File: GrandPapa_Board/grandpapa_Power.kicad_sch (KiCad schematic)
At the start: 47 parts, among them J10 Conn_01x03_Female, J7 Conn_01x02_Female, J8 Conn_01x02_Female, J9 Conn_01x02_Female, U1 LD2985BM33R, U2 INA180A4QDBVRQ1, U3 INA180A4QDBVRQ1, U4 LT1576IS8-5#TRPBF, U5 FPF2124, U6 FPF2124, U7 FPF2124, U9 INA180A4QDBVRQ1

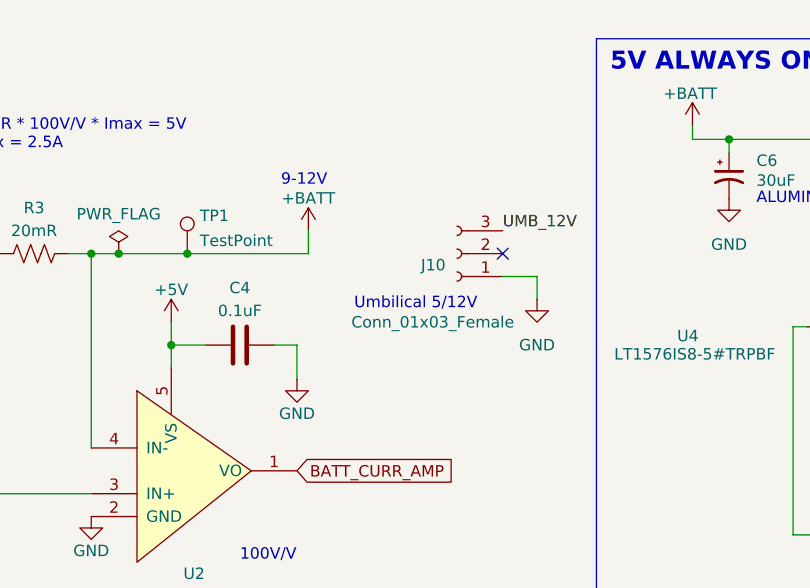
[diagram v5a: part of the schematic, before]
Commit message: Add FETs to power lines
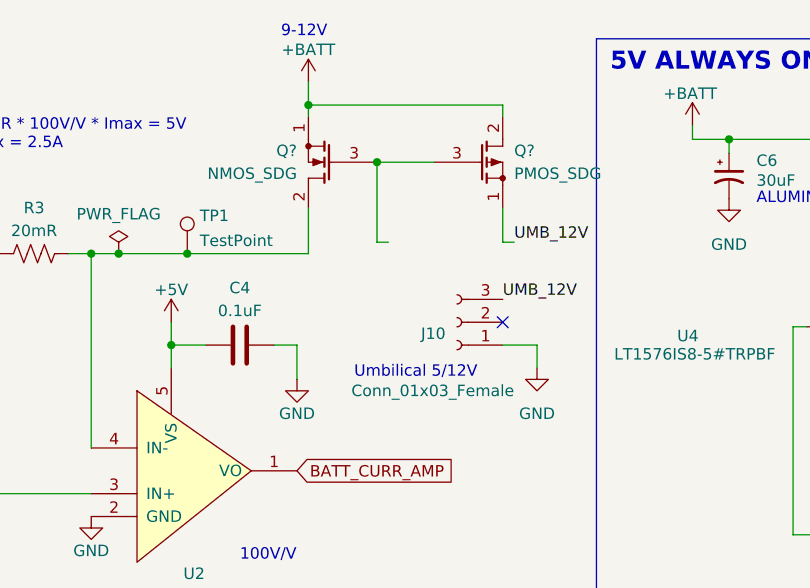
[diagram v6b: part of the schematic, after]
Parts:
- added Q?: PMOS_SDG, symbol CLEAN_MOS:PMOS_SDG
- added Q?: NMOS_SDG, symbol CLEAN_MOS:NMOS_SDG
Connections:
- net +BATT: now also Q?.1 (S), Q?.2 (D); no longer R3.1, TP1.1, U2.4 (IN-)
- net UMB_12V: now also Q?.1 (S)
- new net: Q?.2 (D), R3.1, TP1.1, U2.4 (IN-)
- new net: Q?.3 (G), Q?.3 (G)
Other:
- moved on the sheet: J10
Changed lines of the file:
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@@
   (junction (at 214.122 39.878) (diameter 0) (color 0 0 0 0)
   )
+  (junction (at 120.65 21.59) (diameter 0) (color 0 0 0 0)
+  )
   (junction (at 223.012 52.578) (diameter 0) (color 0 0 0 0)
   )
@@
   (junction (at 256.032 39.878) (diameter 0) (color 0 0 0 0)
   )
+  (junction (at 128.27 27.94) (diameter 0) (color 0 0 0 0)
+  )
   (junction (at 232.41 52.578) (diameter 0) (color 0 0 0 0)
   )
   (junction (at 83.82 38.1) (diameter 0) (color 0 0 0 0)
   )
-  (no_connect (at 142.24 38.1))
+  (no_connect (at 142.24 45.72))
   (wire (pts (xy 181.61 130.81) (xy 172.72 130.81))
     (stroke (width 0) (type default) (color 0 0 0 0))
@@
     (stroke (width 0) (type default) (color 0 0 0 0))
   )
+  (wire (pts (xy 142.24 33.02) (xy 142.24 36.83))
+    (stroke (width 0) (type default) (color 0 0 0 0))
+  )
+  (wire (pts (xy 120.65 19.05) (xy 120.65 21.59))
+    (stroke (width 0) (type default) (color 0 0 0 0))
+  )
   (wire (pts (xy 111.252 173.99) (xy 98.552 173.99))
     (stroke (width 0) (type default) (color 0 0 0 0))
@@
     (stroke (width 0) (type default) (color 0 0 0 0))
   )
-  (wire (pts (xy 142.24 40.64) (xy 146.05 40.64))
+  (wire (pts (xy 142.24 48.26) (xy 146.05 48.26))
     (stroke (width 0) (type default) (color 0 0 0 0))
   )
@@
     (stroke (width 0) (type default) (color 0 0 0 0))
   )
-  (wire (pts (xy 146.05 40.64) (xy 146.05 43.18))
+  (wire (pts (xy 146.05 48.26) (xy 146.05 50.8))
     (stroke (width 0) (type default) (color 0 0 0 0))
   )
@@
     (stroke (width 0) (type default) (color 0 0 0 0))
   )
+  (wire (pts (xy 128.27 27.94) (xy 134.62 27.94))
+    (stroke (width 0) (type default) (color 0 0 0 0))
+  )
   (wire (pts (xy 30.48 66.04) (xy 30.48 76.2))
     (stroke (width 0) (type default) (color 0 0 0 0))
@@
     (stroke (width 0) (type default) (color 0 0 0 0))
   )
+  (wire (pts (xy 120.65 21.59) (xy 142.24 21.59))
+    (stroke (width 0) (type default) (color 0 0 0 0))
+  )
   (wire (pts (xy 30.48 38.1) (xy 46.99 38.1))
     (stroke (width 0) (type default) (color 0 0 0 0))
@@
     (stroke (width 0) (type default) (color 0 0 0 0))
   )
+  (wire (pts (xy 120.65 21.59) (xy 120.65 22.86))
+    (stroke (width 0) (type default) (color 0 0 0 0))
+  )
   (wire (pts (xy 116.078 87.376) (xy 125.222 87.376))
     (stroke (width 0) (type default) (color 0 0 0 0))
@@
     (stroke (width 0) (type default) (color 0 0 0 0))
   )
+  (wire (pts (xy 142.24 22.86) (xy 142.24 21.59))
+    (stroke (width 0) (type default) (color 0 0 0 0))
+  )
+  (wire (pts (xy 142.24 36.83) (xy 143.51 36.83))
+    (stroke (width 0) (type default) (color 0 0 0 0))
+  )
   (wire (pts (xy 101.092 114.046) (xy 88.392 114.046))
     (stroke (width 0) (type default) (color 0 0 0 0))
@@
     (stroke (width 0) (type default) (color 0 0 0 0))
   )
+  (wire (pts (xy 128.27 36.83) (xy 129.54 36.83))
+    (stroke (width 0) (type default) (color 0 0 0 0))
+  )
   (wire (pts (xy 243.84 88.138) (xy 243.84 90.17))
     (stroke (width 0) (type default) (color 0 0 0 0))
@@
     (stroke (width 0) (type default) (color 0 0 0 0))
   )
-  (wire (pts (xy 120.65 35.56) (xy 120.65 38.1))
+  (wire (pts (xy 120.65 33.02) (xy 120.65 38.1))
     (stroke (width 0) (type default) (color 0 0 0 0))
   )
@@
   )
   (wire (pts (xy 107.188 38.1) (xy 120.65 38.1))
+    (stroke (width 0) (type default) (color 0 0 0 0))
+  )
+  (wire (pts (xy 128.27 27.94) (xy 128.27 36.83))
     (stroke (width 0) (type default) (color 0 0 0 0))
   )
@@
     (effects (font (size 1.27 1.27)) (justify left bottom))
   )
-  (text "Umbilical 5/12V" (at 125.73 44.45 0)
+  (text "Umbilical 5/12V" (at 125.73 52.07 0)
     (effects (font (size 1.27 1.27)) (justify left bottom))
   )
@@
     (effects (font (size 1.27 1.27)) (justify left bottom))
   )
-  (text "9-12V\n" (at 117.602 30.734 0)
+  (text "9-12V\n" (at 117.602 14.224 0)
     (effects (font (size 1.27 1.27)) (justify left bottom))
   )
@@
     (effects (font (size 1.27 1.27)) (justify left bottom))
   )
-  (label "UMB_12V" (at 142.24 35.56 0)
+  (label "UMB_12V" (at 142.24 43.18 0)
     (effects (font (size 1.27 1.27)) (justify left bottom))
   )
   (label "RAW_BATT" (at 74.168 35.306 180)
     (effects (font (size 1.27 1.27)) (justify right bottom))
+  )
+  (label "UMB_12V" (at 143.51 36.83 0)
+    (effects (font (size 1.27 1.27)) (justify left bottom))
   )
   (global_label "5V_LOGGER" (shape input) (at 243.84 88.138 0) (fields_autoplaced)
@@
     (pin "5")
   )
-  (symbol (lib_id "power:GND") (at 146.05 43.18 0) (unit 1)
-    (in_bom yes) (on_board yes) (fields_autoplaced)
-    (property "Reference" "#PWR08" (id 0) (at 146.05 49.53 0)
-      (effects (font (size 1.27 1.27)) hide)
-    )
-    (property "Value" "GND" (id 1) (at 146.05 48.26 0))
-    (property "Footprint" "" (id 2) (at 146.05 43.18 0)
-      (effects (font (size 1.27 1.27)) hide)
-    )
-    (property "Datasheet" "" (id 3) (at 146.05 43.18 0)
+  (symbol (lib_id "power:GND") (at 146.05 50.8 0) (unit 1)
+    (in_bom yes) (on_board yes) (fields_autoplaced)
+    (property "Reference" "#PWR08" (id 0) (at 146.05 57.15 0)
+      (effects (font (size 1.27 1.27)) hide)
+    )
+    (property "Value" "GND" (id 1) (at 146.05 55.88 0))
+    (property "Footprint" "" (id 2) (at 146.05 50.8 0)
+      (effects (font (size 1.27 1.27)) hide)
+    )
+    (property "Datasheet" "" (id 3) (at 146.05 50.8 0)
       (effects (font (size 1.27 1.27)) hide)
     )
@@
     (pin "5")
   )
+  (symbol (lib_id "CLEAN_MOS:PMOS_SDG") (at 139.7 27.94 0) (unit 1)
+    (in_bom yes) (on_board yes) (fields_autoplaced)
+    (property "Reference" "Q?" (id 0) (at 143.51 26.6699 0)
+      (effects (font (size 1.27 1.27)) (justify left))
+    )
+    (property "Value" "PMOS_SDG" (id 1) (at 143.51 29.2099 0)
+      (effects (font (size 1.27 1.27)) (justify left))
+    )
+    (property "Footprint" "" (id 2) (at 144.78 25.4 0)
+      (effects (font (size 1.27 1.27)) hide)
+    )
+    (property "Datasheet" "~" (id 3) (at 139.7 27.94 0)
+      (effects (font (size 1.27 1.27)) hide)
+    )
+    (pin "1")
+    (pin "2")
+    (pin "3")
+  )
   (symbol (lib_id "power:GND") (at 214.63 157.48 0) (unit 1)
     (in_bom yes) (on_board yes) (fields_autoplaced)
@@
     (pin "1")
   )
-  (symbol (lib_id "power:+BATT") (at 120.65 35.56 0) (unit 1)
-    (in_bom yes) (on_board yes) (fields_autoplaced)
-    (property "Reference" "#PWR015" (id 0) (at 120.65 39.37 0)
-      (effects (font (size 1.27 1.27)) hide)
-    )
-    (property "Value" "+BATT" (id 1) (at 120.65 31.9555 0))
-    (property "Footprint" "" (id 2) (at 120.65 35.56 0)
-      (effects (font (size 1.27 1.27)) hide)
-    )
-    (property "Datasheet" "" (id 3) (at 120.65 35.56 0)
+  (symbol (lib_id "power:+BATT") (at 120.65 19.05 0) (unit 1)
+    (in_bom yes) (on_board yes) (fields_autoplaced)
+    (property "Reference" "#PWR015" (id 0) (at 120.65 22.86 0)
+      (effects (font (size 1.27 1.27)) hide)
+    )
+    (property "Value" "+BATT" (id 1) (at 120.65 15.4455 0))
+    (property "Footprint" "" (id 2) (at 120.65 19.05 0)
+      (effects (font (size 1.27 1.27)) hide)
+    )
+    (property "Datasheet" "" (id 3) (at 120.65 19.05 0)
       (effects (font (size 1.27 1.27)) hide)
     )
@@
     (pin "1")
   )
-  (symbol (lib_id "Connector:Conn_01x03_Female") (at 137.16 38.1 180) (unit 1)
-    (in_bom yes) (on_board yes)
-    (property "Reference" "J10" (id 0) (at 135.89 39.3701 0)
-      (effects (font (size 1.27 1.27)) (justify left))
-    )
-    (property "Value" "Conn_01x03_Female" (id 1) (at 143.51 45.72 0)
-      (effects (font (size 1.27 1.27)) (justify left))
-    )
-    (property "Footprint" "" (id 2) (at 137.16 38.1 0)
-      (effects (font (size 1.27 1.27)) hide)
-    )
-    (property "Datasheet" "~" (id 3) (at 137.16 38.1 0)
+  (symbol (lib_id "Connector:Conn_01x03_Female") (at 137.16 45.72 180) (unit 1)
+    (in_bom yes) (on_board yes)
+    (property "Reference" "J10" (id 0) (at 135.89 46.9901 0)
+      (effects (font (size 1.27 1.27)) (justify left))
+    )
+    (property "Value" "Conn_01x03_Female" (id 1) (at 143.51 53.34 0)
+      (effects (font (size 1.27 1.27)) (justify left))
+    )
+    (property "Footprint" "" (id 2) (at 137.16 45.72 0)
+      (effects (font (size 1.27 1.27)) hide)
+    )
+    (property "Datasheet" "~" (id 3) (at 137.16 45.72 0)
       (effects (font (size 1.27 1.27)) hide)
     )
@@
     (pin "1")
   )
+  (symbol (lib_id "CLEAN_MOS:NMOS_SDG") (at 123.19 27.94 180) (unit 1)
+    (in_bom yes) (on_board yes) (fields_autoplaced)
+    (property "Reference" "Q?" (id 0) (at 119.38 26.6699 0)
+      (effects (font (size 1.27 1.27)) (justify left))
+    )
+    (property "Value" "NMOS_SDG" (id 1) (at 119.38 29.2099 0)
+      (effects (font (size 1.27 1.27)) (justify left))
+    )
+    (property "Footprint" "" (id 2) (at 118.11 30.48 0)
+      (effects (font (size 1.27 1.27)) hide)
+    )
+    (property "Datasheet" "~" (id 3) (at 123.19 27.94 0)
+      (effects (font (size 1.27 1.27)) hide)
+    )
+    (pin "1")
+    (pin "2")
+    (pin "3")
+  )
 )

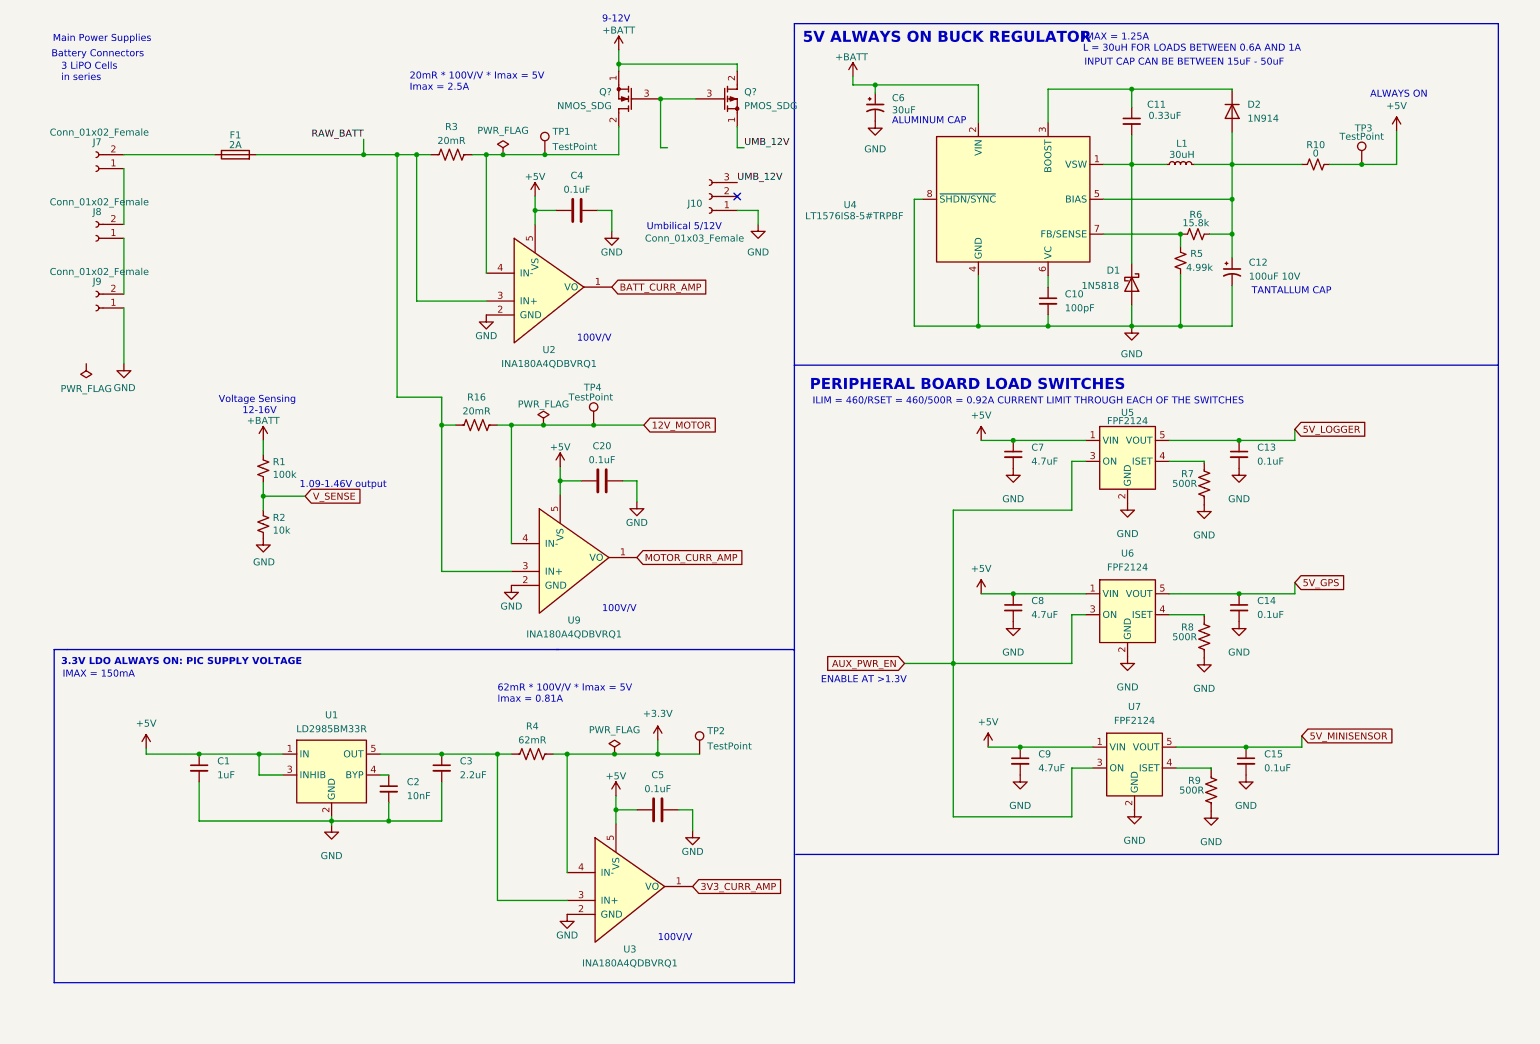
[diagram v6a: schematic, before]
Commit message: clean up schematic, edit nets for clarification, add gnd test points, edit load switching scheme
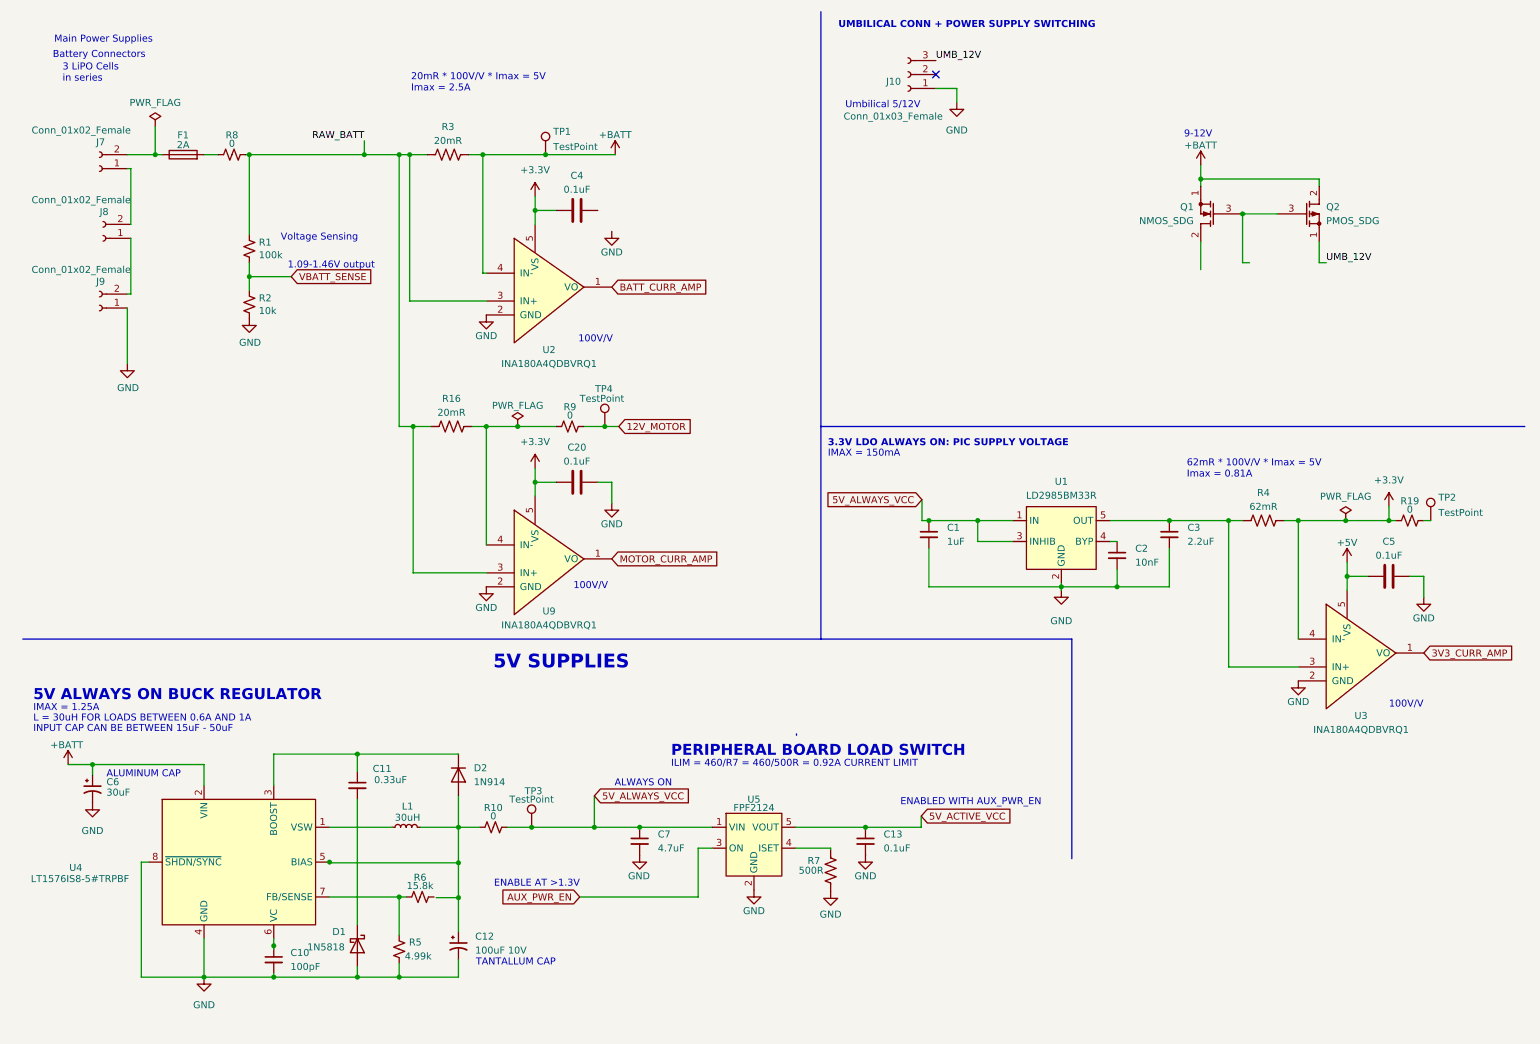
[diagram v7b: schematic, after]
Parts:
- removed C14, C15: 0.1uF, symbol Device:C_Small
- removed C8, C9: 4.7uF, symbol Device:C_Small
- removed R8, R9: 500R, Resistor_SMD:R_1206_3216Metric_Pad1.30x1.75mm_HandSolder, symbol Device:R_US
- removed U6, U7: FPF2124, symbol grandpapa board:FPF2124
- added R19, R8, R9: 0, symbol Device:R_Small_US
- gave numbers to parts that had none: 2
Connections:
- net +3V3: now also C20.2, C4.2, U2.5 (VS), U9.5 (VS), R19.1; no longer TP2.1
- net +5V: no longer C1.1, C20.2, C4.2, C7.1, R10.2, TP3.1, U1.1 (IN), U1.3 (INHIB), U2.5 (VS), U5.1 (VIN), U9.5 (VS)
- net +BATT: now also R3.1, TP1.1, U2.4 (IN-); no longer R1.1
- net 12V_MOTOR: now also R9.2; no longer R16.1, U9.4 (IN-)
- net GND: no longer C4.1
- net RAW_BATT: now also R1.1, R8.2; no longer F1.2
- net at C12.1, D2.2 (A), L1.2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: no longer R6.2, U4.5 (BIAS)
- net at L1.1, U4.1 (VSW): no longer C11.2, D1.1 (K)
- net 5V_LOGGER renamed 5V_ACTIVE_VCC
- net V_SENSE renamed VBATT_SENSE
- new net: R16.1, R9.1, U9.4 (IN-)
- new net: F1.2, R8.1
- new net: R19.2, TP2.1
- new net: C11.2, D1.1 (K)
- new net 5V_ALWAYS_VCC: C1.1, C7.1, R10.2, TP3.1, U1.1 (IN), U1.3 (INHIB), U5.1 (VIN)
- now unconnected: Q1.2 (D)
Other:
- note added: "5V SUPPLIES"
- note added: "ENABLED WITH AUX_PWR_EN"
- note added: "ILIM = 460/R7 = 460/500R = 0.92A CURRENT LIMIT"
- note added: "PERIPHERAL BOARD LOAD SWITCH"
- note added: "UMBILICAL CONN + POWER SUPPLY SWITCHING"
- note removed: "12-16V"
- note removed: "ILIM = 460/RSET = 460/500R = 0.92A CURRENT LIMIT THROUGH EACH OF THE SWITCHES"
- note removed: "PERIPHERAL BOARD LOAD SWITCHES"
- moved on the sheet: C1, C10, C11, C12, C13, C2, C20, C3, C5, C6, C7, D1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
